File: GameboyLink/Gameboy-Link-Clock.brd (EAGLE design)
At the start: 56.6 x 34 mm, 38 parts, among them IC1 MEGA8-AI, J1 AVR_SPI_PRG_6PTH, Q1 16MHz, U1 DS1307Z, Y1 32.768kHz

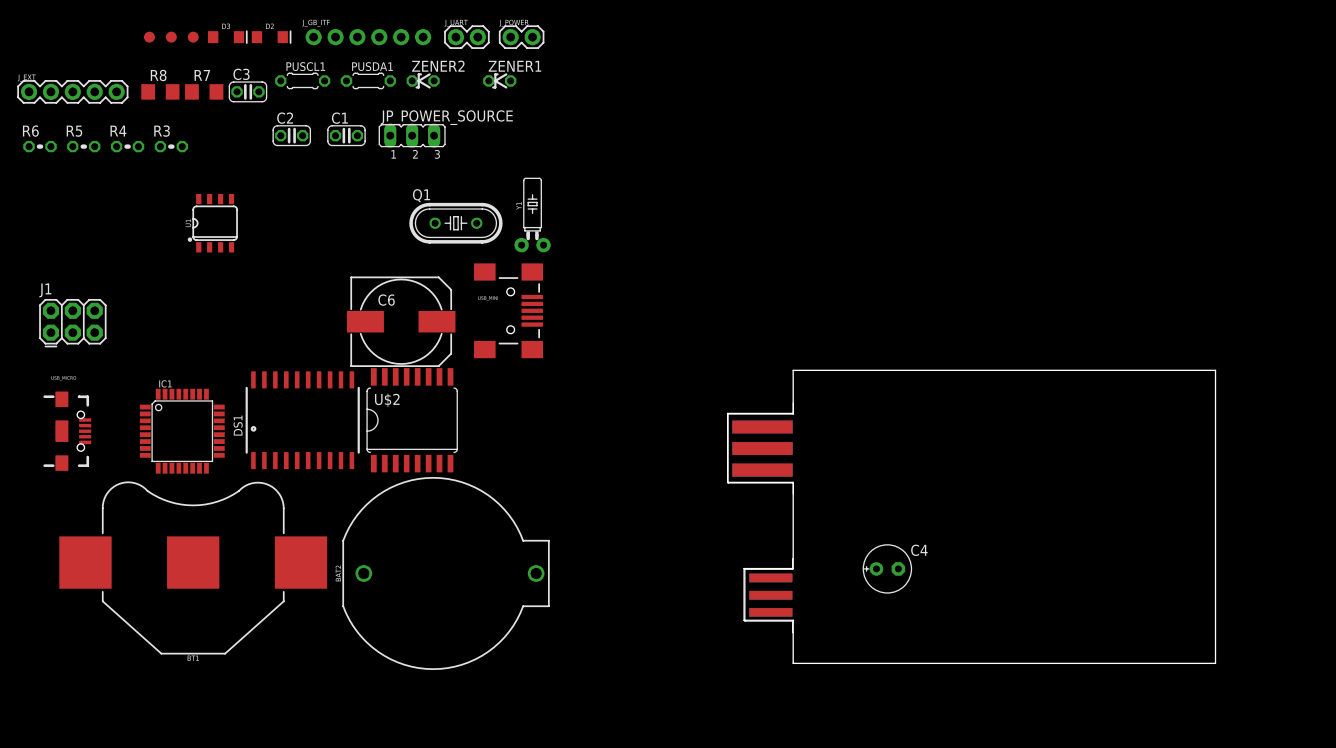
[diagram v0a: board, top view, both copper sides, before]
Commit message: All components on the board, now routing and adjustments.
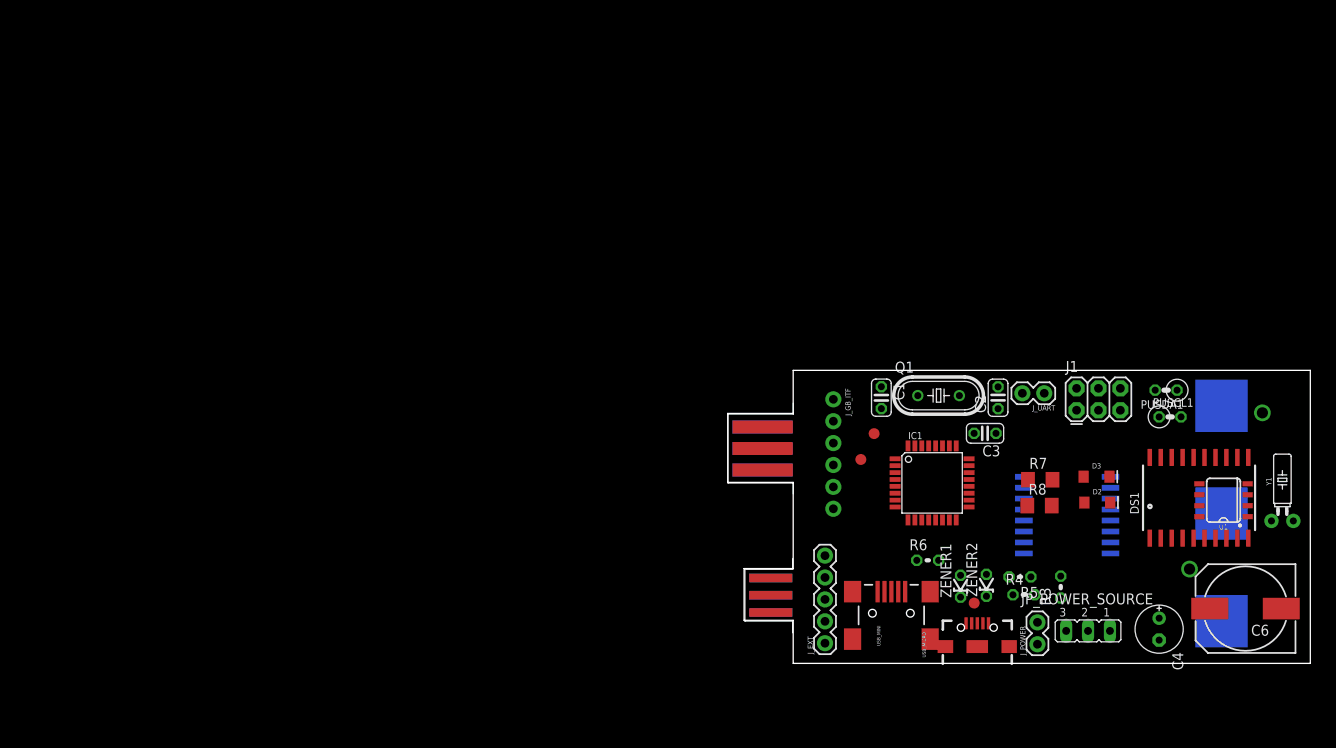
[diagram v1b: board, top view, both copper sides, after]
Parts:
- PUSCL1, PUSDA1: device resistor:0204/5 -> rcl:0207/2V
- moved U1 121.3 mm to (64.9, 19.9), turned to 90 degrees
- moved R5 119.5 mm to (41.3, 11.0), turned to 180 degrees
- moved BT1 119.4 mm to (64.7, 18.4), flipped to the bottom, turned to 90 degrees
- moved J1 119.3 mm to (47.9, 30.4)
- moved R4 116.3 mm to (41.8, 8.96)
- moved TP_USB_ID 116.1 mm to (36.0, 8.00)
- moved R3 115.2 mm to (46.0, 9.85), turned to 90 degrees
- moved R6 113.6 mm to (30.6, 13.0)
- moved D3 113.1 mm to (50.2, 22.7)
- moved R8 112.7 mm to (43.6, 19.3)
- moved J_EXT 112.3 mm to (18.7, 3.34), turned to 90 degrees
- moved D2 110.1 mm to (50.3, 19.7)
- moved USB_MICRO 109.1 mm to (36.4, 2.95), turned to 90 degrees
- moved PUSCL1 107.9 mm to (58.7, 29.6)
- moved R7 106.9 mm to (43.7, 22.3)
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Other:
- board size 56.6 x 34 mm -> 67.6 x 34 mm

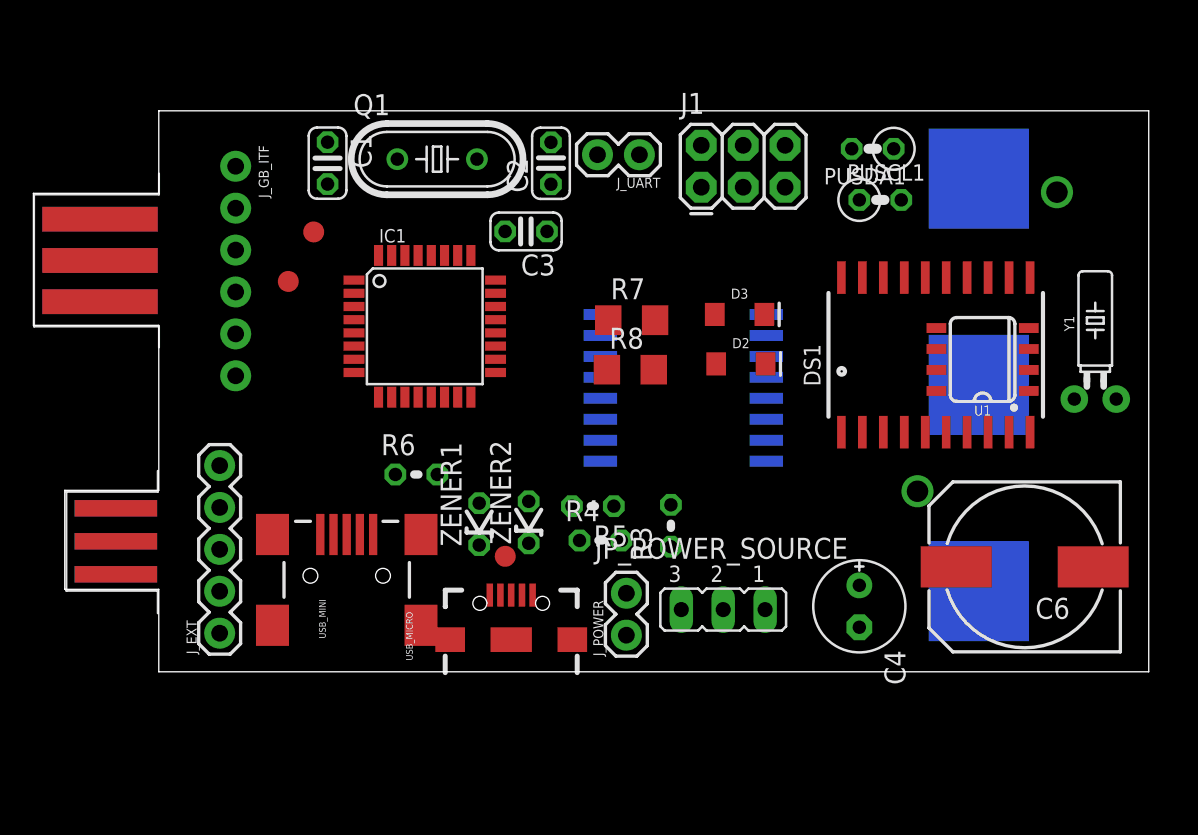
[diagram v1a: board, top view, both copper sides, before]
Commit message: Roudned corners on the GBC connector side of the board... a pain to do!
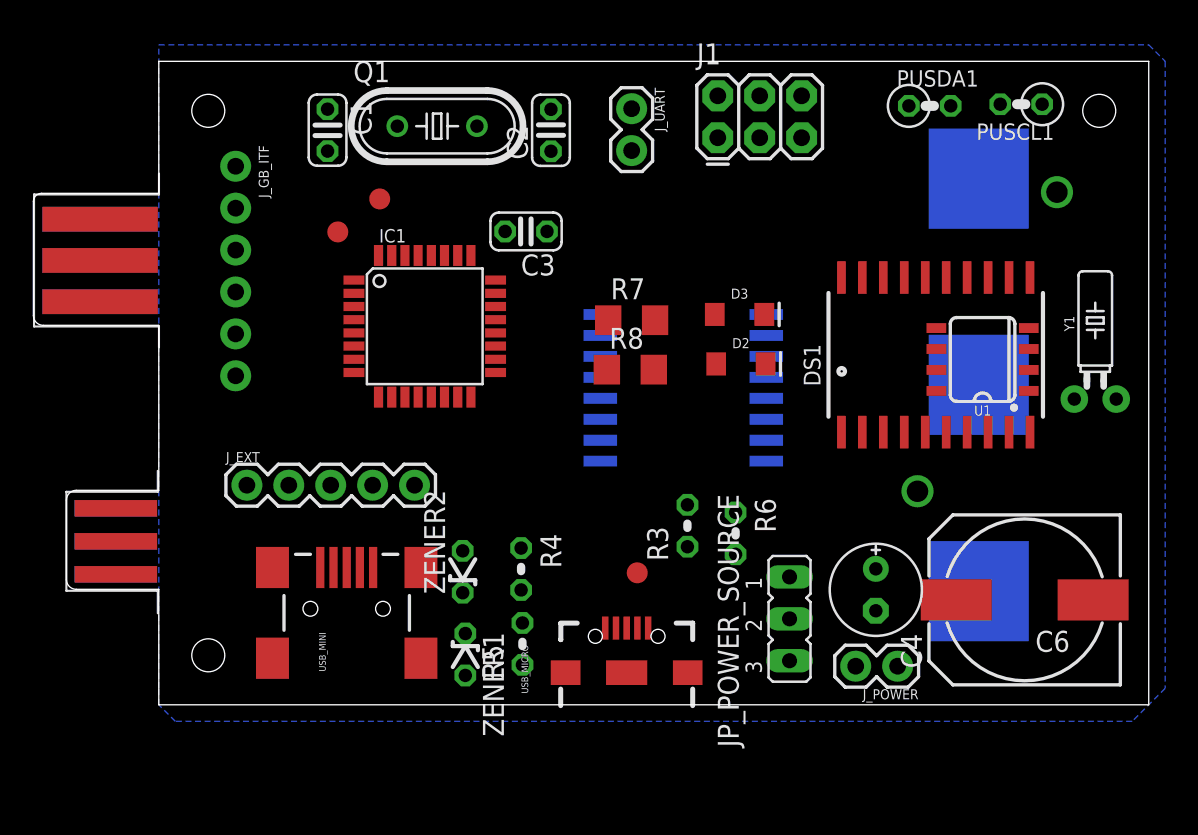
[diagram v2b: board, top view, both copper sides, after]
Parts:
- moved R6 19.7 mm to (50.0, 9.39), turned to 270 degrees
- moved J_POWER 16.5 mm to (59.8, 1.34), turned to 180 degrees
- moved PUSCL1 10.3 mm to (67.3, 35.4), turned to 180 degrees
- moved R5 9.38 mm to (37.0, 2.69), turned to 90 degrees
- moved J_EXT 9.12 mm to (20.3, 12.3), turned to 0 degrees
- moved TP_USB_ID 8.06 mm to (44.0, 7.00)
- moved ZENER1 7.94 mm to (33.6, 2.05), turned to 270 degrees
- moved USB_MICRO 7.28 mm to (43.4, 0.95)
- moved R4 5.11 mm to (37.0, 7.23), turned to 270 degrees
- moved ZENER2 5.00 mm to (33.4, 7.06)
- moved JP_D+ 4.47 mm to (28.4, 29.7)
- moved PUSDA1 4.33 mm to (61.7, 35.3), turned to 0 degrees
- moved JP_D- 4.24 mm to (25.9, 27.7)
- moved JP_POWER_SOURCE 4.06 mm to (53.2, 4.21), turned to 270 degrees
- moved J1 3.16 mm to (48.9, 33.4)
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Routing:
- added copper zone on layer 16, net GND
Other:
- board size 67.6 x 34 mm -> 67.6 x 39 mm

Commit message: Before manual routing
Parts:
- removed DS1: DS3234, SparkFun:DS3234
- removed JP_D+, JP_D-: (no value), SparkFun-Passives:PAD.03X.05
- removed J_GB_ITF: (no value), SparkFun-Connectors:1X06_NO_SILK
- added J_GB_DBG: FEMALE 2x3, SparkFun-Connectors:2X3
- added R1, R2: 10k, rcl:R1206
- moved D3 26.0 mm to (24.8, 28.3), turned to 180 degrees
- moved D2 26.0 mm to (24.7, 24.3), turned to 180 degrees
- moved J_EXT 22.6 mm to (36.3, 28.4), turned to 270 degrees
- moved Y1 21.7 mm to (50.5, 13.2), turned to 270 degrees
- moved U$2 19.5 mm to (66.2, 19.1), flipped to the top
- moved C1 19.0 mm to (44.2, 33.8)
- moved R7 14.8 mm to (30.3, 28.7), turned to 180 degrees
- moved C3 14.5 mm to (42.7, 14.3), turned to 0 degrees
- moved R8 14.2 mm to (30.4, 24.7), turned to 180 degrees
- moved R3 13.3 mm to (34.0, 12.8)
- moved R6 13.3 mm to (37.0, 12.6), turned to 90 degrees
- moved IC1 12.8 mm to (43.9, 21.9), turned to 270 degrees
- moved J_UART 12.7 mm to (52.3, 25.9), turned to 90 degrees
- moved U1 11.0 mm to (53.9, 19.1), turned to 0 degrees
- moved C2 9.00 mm to (29.8, 33.8)
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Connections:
- removed net N$9: DS1.1, IC1.14
- net BATP: no longer DS1.16
- net D+: no longer JP_D+.P$1
- net D-: no longer JP_D-.P$1
- net GB_CLK: now also J_GB_DBG.5; no longer J_GB_ITF.5
- net GB_MISO: now also J_GB_DBG.3; no longer J_GB_ITF.3
- net GB_MOSI: now also J_GB_DBG.2; no longer J_GB_ITF.2
- net GB_SD: now also J_GB_DBG.4; no longer J_GB_ITF.4
- net GB_VCC: now also J_GB_DBG.1; no longer J_GB_ITF.1
- net GND: now also J_GB_DBG.6; no longer DS1.10, DS1.11, DS1.12, DS1.13, DS1.14, DS1.15, DS1.2, DS1.7, DS1.8, DS1.9, J_GB_ITF.6
- net N$1: now also R2.1
- net N$2: now also R1.1
- net N$3: no longer DS1.18, DS1.20
- net N$7: no longer DS1.17
- net N$8: no longer DS1.19
- net RESET: no longer DS1.6
- net VCC: now also R1.2, R2.2; no longer DS1.4

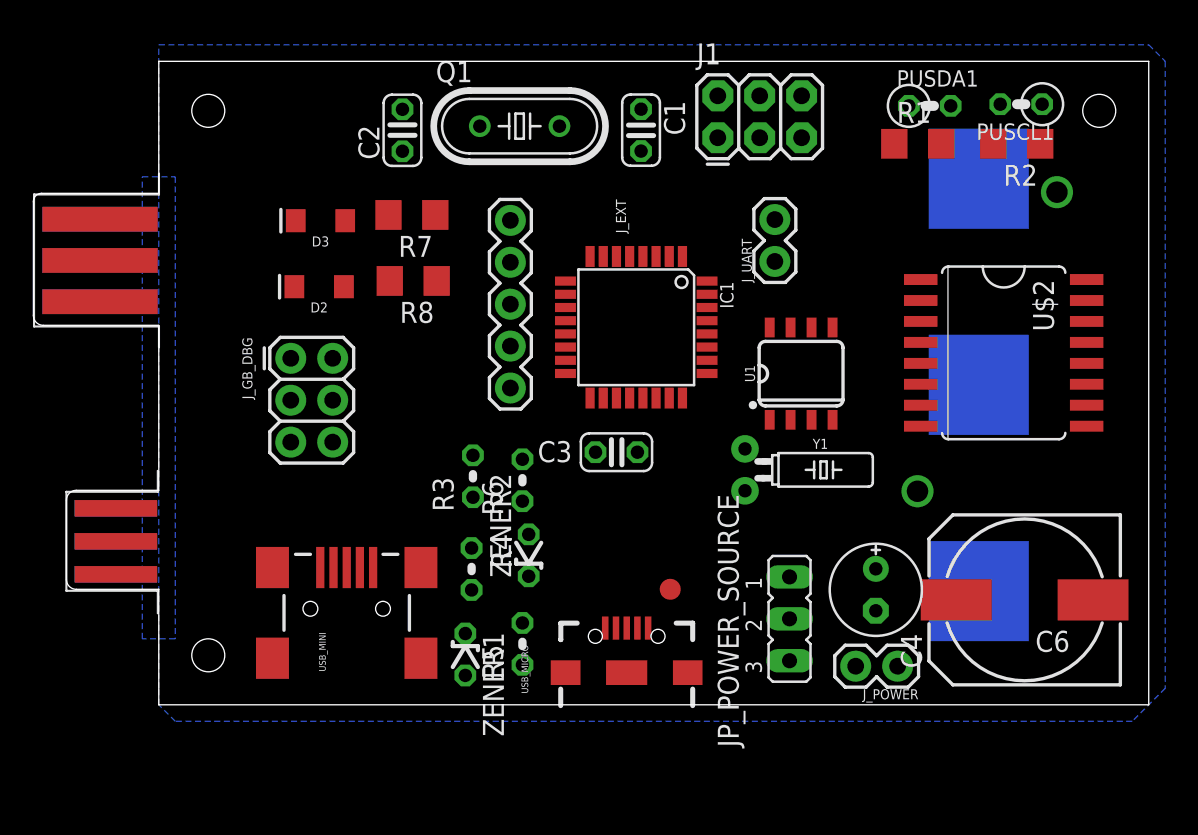
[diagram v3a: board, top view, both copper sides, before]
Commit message: Powers line done. Just noticed I forgot to wire ... THE GB LINK PORT to the MCU!!
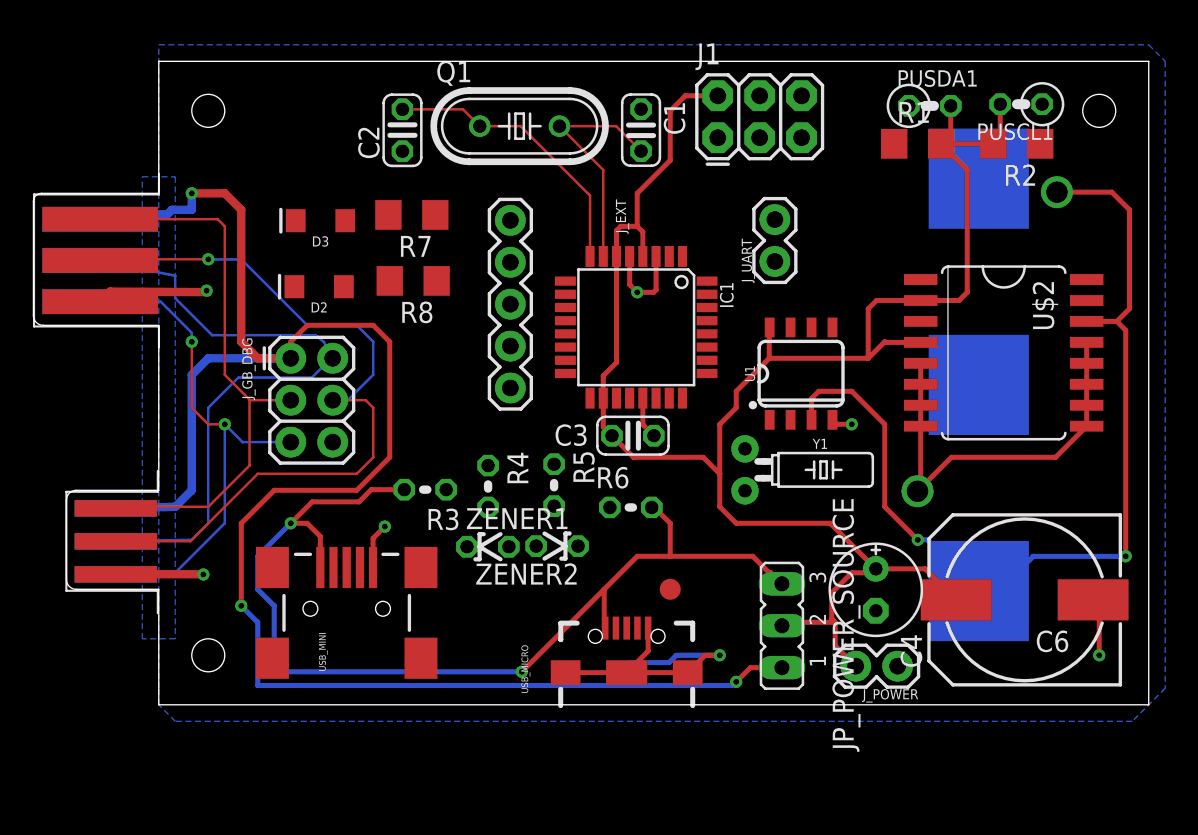
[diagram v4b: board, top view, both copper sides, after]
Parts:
- moved R5 9.81 mm to (39.0, 12.3), turned to 270 degrees
- moved R6 6.77 mm to (43.6, 11.0), turned to 0 degrees
- moved ZENER1 6.67 mm to (35.0, 8.58), turned to 0 degrees
- moved R4 5.10 mm to (35.0, 12.2)
- moved R3 3.00 mm to (31.1, 12.0), turned to 180 degrees
- moved ZENER2 1.81 mm to (39.1, 8.62), turned to 180 degrees
- moved C3 1.41 mm to (43.7, 15.3)
- moved JP_POWER_SOURCE 0.62 mm to (52.8, 3.79), turned to 90 degrees
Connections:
- net USB_VCC: now also USB_MINI.VBUS
- net VCC: no longer USB_MINI.VBUS
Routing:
- net VCC: track 0.00 -> 112.3 mm
- net GB_VCC: track 0.00 -> 108.1 mm, vias 0 -> 3
- net GND: track 0.00 -> 71.7 mm, vias 0 -> 7
- net USB_VCC: track 0.00 -> 62.2 mm, vias 0 -> 2
- net BATP: track 0.00 -> 57.8 mm, vias 0 -> 2
- net GB_SD: track 0.00 -> 47.1 mm, vias 0 -> 1
- net GB_MOSI: track 0.00 -> 39.0 mm
- net GB_MISO: track 0.00 -> 34.5 mm
- net GB_CLK: track 0.00 -> 32.0 mm, vias 0 -> 2
- net N$5: track 0.00 -> 17.2 mm
- net N$4: track 0.00 -> 14.6 mm

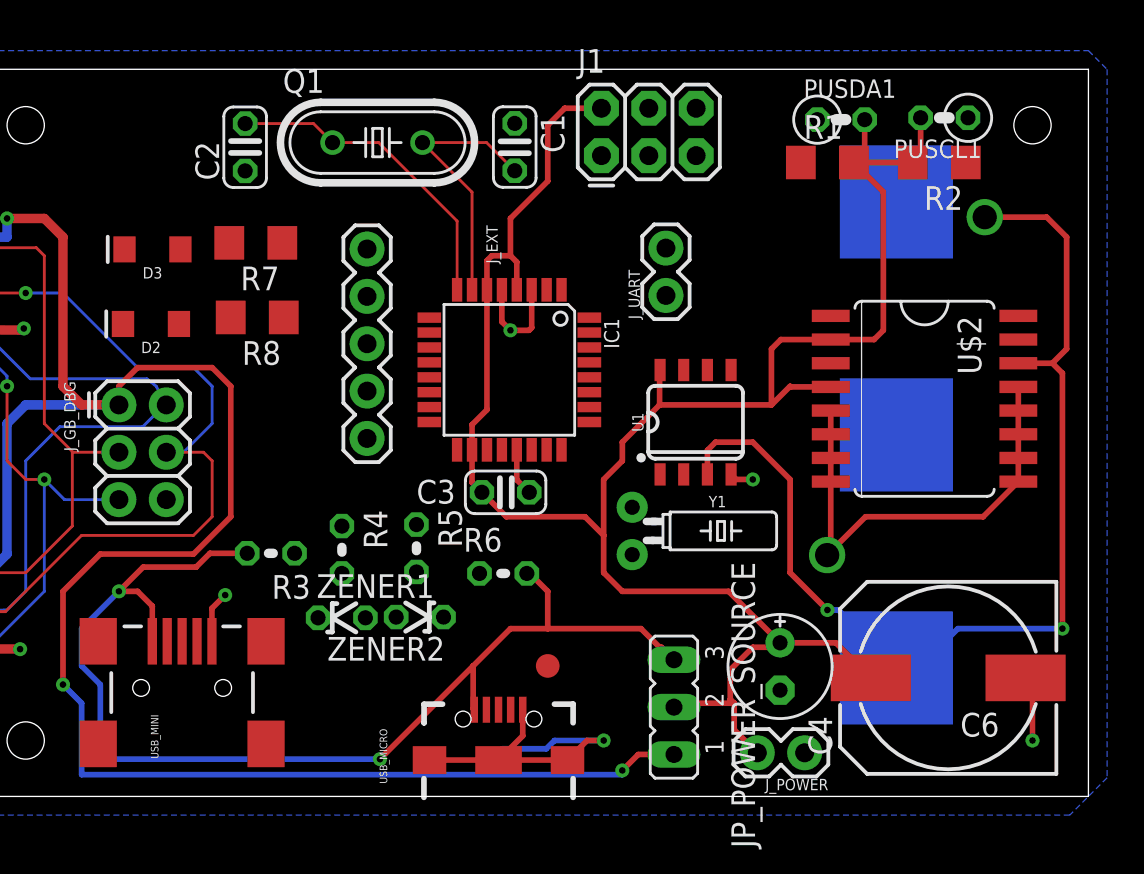
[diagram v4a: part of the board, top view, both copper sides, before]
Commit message: All routed minus USB and ISP
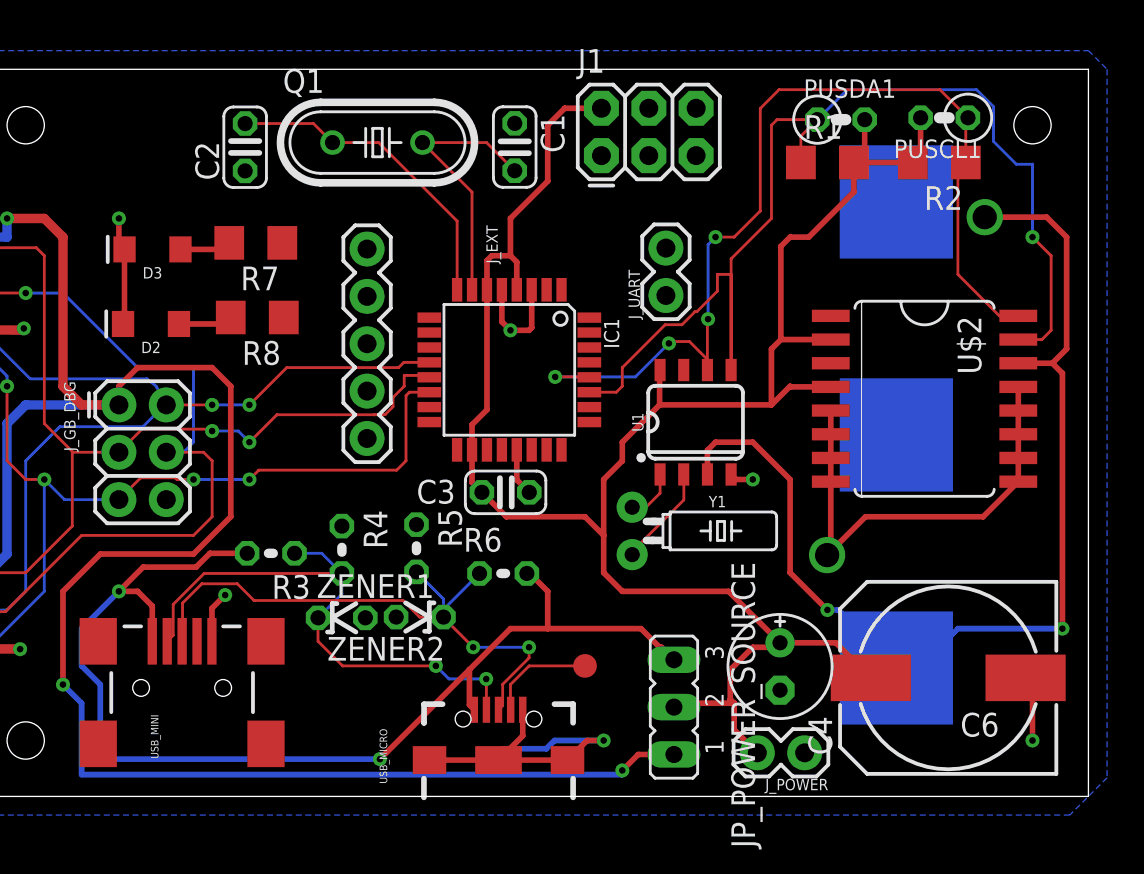
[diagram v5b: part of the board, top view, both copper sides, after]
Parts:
- moved TP_USB_ID 2.00 mm to (48.0, 6.00)
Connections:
- net GB_CLK: now also IC1.14
- net GB_MISO: now also IC1.13
- net GB_MOSI: now also IC1.12
- net N$21: now also IC1.19; no longer IC1.12
- net N$22: now also IC1.22; no longer IC1.13
- net N$23: now also Y1.1; no longer Y1.2
- net N$24: now also Y1.2; no longer Y1.1
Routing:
- net N$2: track 0.00 -> 62.0 mm, vias 0 -> 1
- net N$1: track 0.00 -> 52.6 mm, vias 0 -> 4
- net USBD+: track 0.00 -> 32.7 mm, vias 0 -> 2
- net USBD-: track 0.00 -> 30.5 mm, vias 0 -> 2
- net GB_CLK: track 32.0 -> 53.1 mm, vias 2 -> 4
- net GB_MISO: track 34.5 -> 54.2 mm, vias 0 -> 2
- net GB_MOSI: track 39.0 -> 54.1 mm, vias 0 -> 2
- net GND: track 71.7 -> 77.5 mm, vias 7 -> 8
- net N$14: track 0.00 -> 5.77 mm
- net N$24: track 0.00 -> 5.45 mm
- net N$19: track 0.00 -> 2.92 mm
- net N$23: track 0.00 -> 2.81 mm
- net N$20: track 0.00 -> 2.76 mm
- net VCC: track 112.3 -> 111.3 mm
- net GB_SD: track 47.1 -> 46.3 mm
